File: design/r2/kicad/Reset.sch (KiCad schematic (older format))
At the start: 13 parts, among them IC15 555N, J23 RESET_SW

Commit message: Tidy up footprints
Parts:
- removed J23: RESET_SW, Connector_PinHeader_2.54mm:PinHeader_2x01_P2.54mm_Vertical, symbol Connector:Conn_01x02_Male
- C20: footprint rosco_m68k:C-Electolytic-2,5-5 -> rosco_m68k:E2,5-5
- R27, R28, R29, R30, R31, R32: footprint rosco_m68k:R-0207_10 -> rosco_m68k:0207_10
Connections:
- wire segments 53 -> 47
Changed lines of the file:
@@
 $Descr A4 11693 8268
 encoding utf-8
-Sheet 5 7
+Sheet 4 7
 Title "rosco_m68k Pro (030) Prototype"
 Date "2021-10-01"
@@
 	7450 3200 7450 3000
 Wire Wire Line
-	3350 5200 3450 5200
-Wire Wire Line
 	3850 3800 4150 3800
 Wire Wire Line
@@
 Wire Wire Line
 	1650 4900 1650 3400
-Wire Wire Line
-	2950 5200 2650 5200
 Wire Wire Line
 	2350 5200 2350 4900
@@
 F 0 "R27" V 2191 2750 59  0000 L BNN
 F 1 "2K2" V 2080 2750 59  0000 L BNN
-F 2 "rosco_m68k:R-0207_10" H 2050 2700 50  0001 C CNN
+F 2 "rosco_m68k:0207_10" H 2050 2700 50  0001 C CNN
 F 3 "" H 2050 2700 50  0001 C CNN
 	1    2050 2700
@@
 F 0 "R28" H 3700 5050 59  0000 L BNN
 F 1 "270R" H 3650 5300 59  0000 L BNN
-F 2 "rosco_m68k:R-0207_10" H 3750 5200 50  0001 C CNN
+F 2 "rosco_m68k:0207_10" H 3750 5200 50  0001 C CNN
 F 3 "" H 3750 5200 50  0001 C CNN
 	1    3750 5200
@@
 F 0 "R30" V 8191 2850 59  0000 L BNN
 F 1 "330R" V 8080 2850 59  0000 L BNN
-F 2 "rosco_m68k:R-0207_10" H 8050 2800 50  0001 C CNN
+F 2 "rosco_m68k:0207_10" H 8050 2800 50  0001 C CNN
 F 3 "" H 8050 2800 50  0001 C CNN
 	1    8050 2800
@@
 F 0 "R31" V 8641 2850 59  0000 L BNN
 F 1 "4K7" V 8530 2850 59  0000 L BNN
-F 2 "rosco_m68k:R-0207_10" H 8500 2800 50  0001 C CNN
+F 2 "rosco_m68k:0207_10" H 8500 2800 50  0001 C CNN
 F 3 "" H 8500 2800 50  0001 C CNN
 	1    8500 2800
@@
 F 0 "R32" V 9291 2850 59  0000 L BNN
 F 1 "4K7" V 9180 2850 59  0000 L BNN
-F 2 "rosco_m68k:R-0207_10" H 9150 2800 50  0001 C CNN
+F 2 "rosco_m68k:0207_10" H 9150 2800 50  0001 C CNN
 F 3 "" H 9150 2800 50  0001 C CNN
 	1    9150 2800
@@
 F 0 "R29" V 7591 2850 59  0000 L BNN
 F 1 "330R" V 7480 2850 59  0000 L BNN
-F 2 "rosco_m68k:R-0207_10" H 7450 2800 50  0001 C CNN
+F 2 "rosco_m68k:0207_10" H 7450 2800 50  0001 C CNN
 F 3 "" H 7450 2800 50  0001 C CNN
 	1    7450 2800
@@
 AR Path="/60FBFA5C/6104F05A" Ref="LED?"  Part="1"
 AR Path="/61043B8D/6104F05A" Ref="LED2"  Part="1"
-AR Path="/6162E38E/6104F05A" Ref="LED2"  Part="1"
-F 0 "LED2" H 8300 3400 59  0000 R TNN
+AR Path="/6162E38E/6104F05A" Ref="LED4"  Part="1"
+F 0 "LED4" H 8300 3400 59  0000 R TNN
 F 1 "RED" H 8300 3300 59  0000 R TNN
 F 2 "rosco_m68k:LED5MM" H 8050 3300 50  0001 C CNN
@@
 AR Path="/60FBFA5C/6104F060" Ref="LED?"  Part="1"
 AR Path="/61043B8D/6104F060" Ref="LED1"  Part="1"
-AR Path="/6162E38E/6104F060" Ref="LED1"  Part="1"
-F 0 "LED1" H 7700 3400 59  0000 R TNN
+AR Path="/6162E38E/6104F060" Ref="LED3"  Part="1"
+F 0 "LED3" H 7700 3400 59  0000 R TNN
 F 1 "GREEN" H 7800 3300 59  0000 R TNN
 F 2 "rosco_m68k:LED5MM" H 7450 3300 50  0001 C CNN
@@
 F 0 "C11" H 2095 4119 59  0000 L BNN
 F 1 "100uF" H 2095 3919 59  0000 L BNN
-F 2 "rosco_m68k:C-Electolytic-2,5-5" H 2050 4100 50  0001 C CNN
+F 2 "rosco_m68k:E2,5-5" H 2050 4100 50  0001 C CNN
 F 3 "" H 2050 4100 50  0001 C CNN
 	1    2050 4100
@@
 Wire Wire Line
 	4500 4800 4800 4800
-Connection ~ 2650 5200
-Wire Wire Line
-	2650 5200 2350 5200
-$Comp
-L Connector:Conn_01x02_Male J23
-U 1 1 6172EF3B
-P 3200 5600
-F 0 "J23" V 3500 5500 50  0000 L CNN
-F 1 "RESET_SW" V 3600 5350 50  0000 L CNN
-F 2 "Connector_PinHeader_2.54mm:PinHeader_2x01_P2.54mm_Vertical" H 3200 5600 50  0001 C CNN
-F 3 "~" H 3200 5600 50  0001 C CNN
-	1    3200 5600
-	0    1    1    0
-$EndComp
-Wire Wire Line
-	3100 5800 2650 5800
-Wire Wire Line
-	2650 5200 2650 5800
-Wire Wire Line
-	3200 5800 3450 5800
-Wire Wire Line
-	3450 5800 3450 5200
-Connection ~ 3450 5200
-Wire Wire Line
-	3450 5200 3550 5200
 Text GLabel 4800 4800 2    50   Output ~ 0
 HWRST
@@
 Text GLabel 6100 3700 0    50   Input ~ 0
 RUNLED
+Wire Wire Line
+	2350 5200 2950 5200
+Wire Wire Line
+	3350 5200 3550 5200
 $EndSCHEMATC

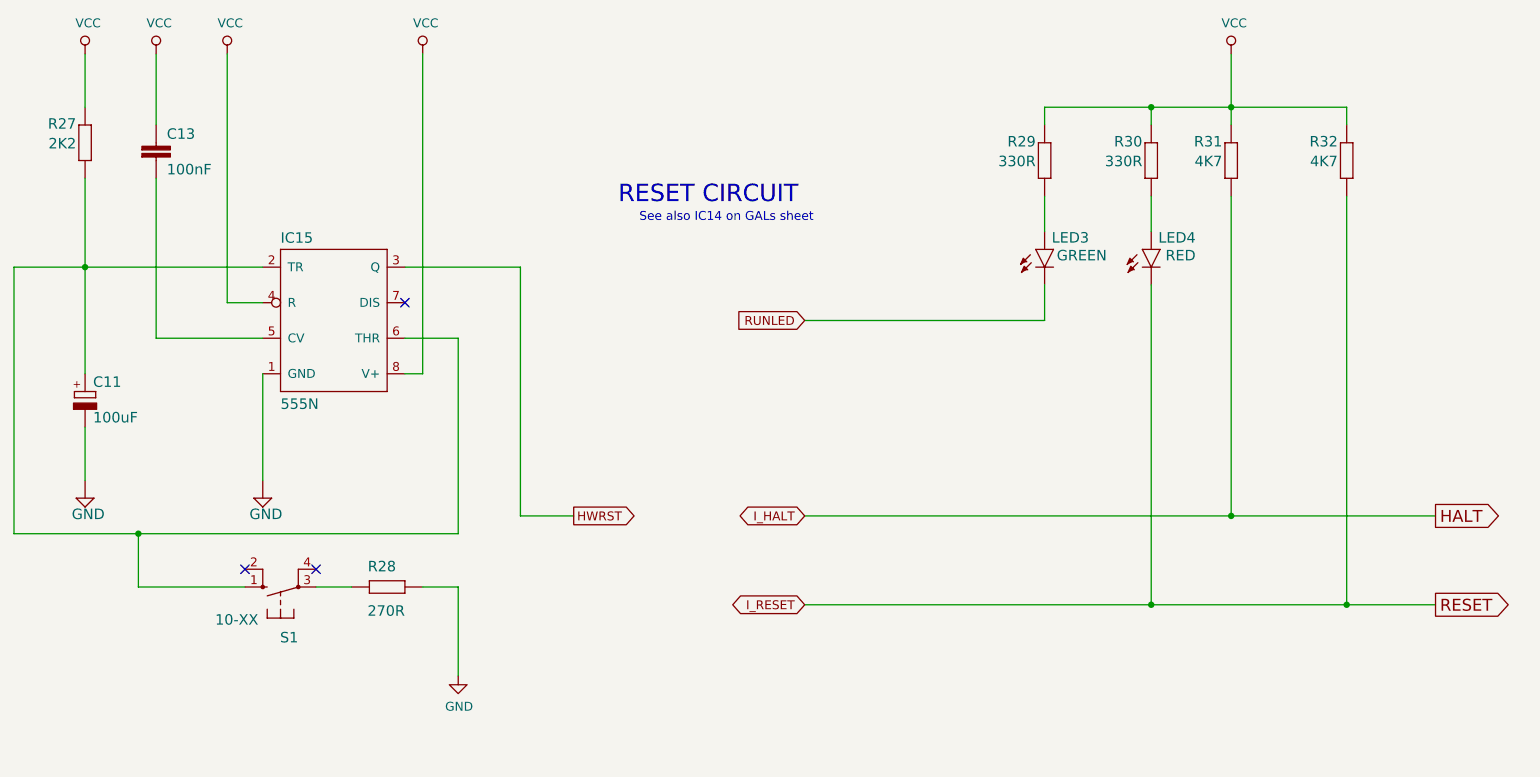
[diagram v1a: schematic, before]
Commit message: Schematic / GAL tweaks and do layout
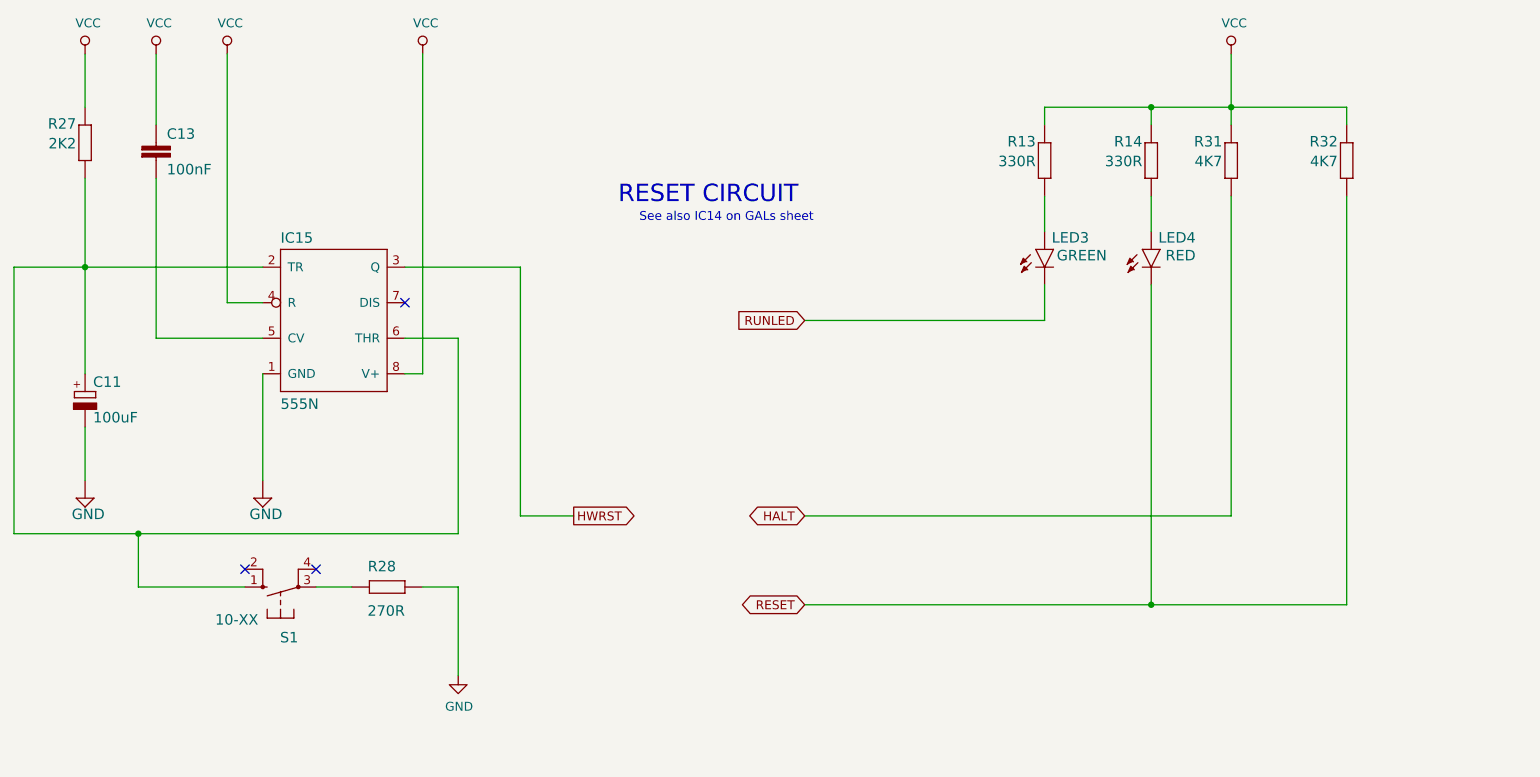
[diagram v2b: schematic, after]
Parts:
- C21: footprint Capacitor_THT:C_Rect_L4.0mm_W2.5mm_P2.50mm -> rosco_m68k:C2.5-3
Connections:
- net I_RESET renamed RESET
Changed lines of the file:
@@
 Wire Wire Line
 	2450 3800 3050 3800
-Text GLabel 9650 4800 2    67   Output ~ 0
-HALT
 Wire Wire Line
 	7450 3700 7450 3500
@@
 Connection ~ 2050 3400
 Connection ~ 2350 4900
-Text GLabel 9650 5300 2    67   Output ~ 0
-RESET
 $Comp
 L rosco_m68k-eagle-import:555N IC?
@@
 AR Path="/60FBFA5C/6104F030" Ref="R?"  Part="1"
 AR Path="/61043B8D/6104F030" Ref="R30"  Part="1"
-AR Path="/6162E38E/6104F030" Ref="R30"  Part="1"
-F 0 "R30" V 8191 2850 59  0000 L BNN
+AR Path="/6162E38E/6104F030" Ref="R14"  Part="1"
+F 0 "R14" V 8191 2850 59  0000 L BNN
 F 1 "330R" V 8080 2850 59  0000 L BNN
 F 2 "rosco_m68k:0207_10" H 8050 2800 50  0001 C CNN
@@
 	1    9150 2800
 	0    -1   -1   0
-$EndComp
-$Comp
-L rosco_m68k-eagle-import:R-EU_0207_10 R?
-U 1 1 6104F042
-P 7450 2800
-AR Path="/6104F042" Ref="R?"  Part="1"
-AR Path="/5E53B952/6104F042" Ref="R?"  Part="1"
-AR Path="/60FBFA5C/6104F042" Ref="R?"  Part="1"
-AR Path="/61043B8D/6104F042" Ref="R29"  Part="1"
-AR Path="/6162E38E/6104F042" Ref="R29"  Part="1"
-F 0 "R29" V 7591 2850 59  0000 L BNN
-F 1 "330R" V 7480 2850 59  0000 L BNN
-F 2 "rosco_m68k:0207_10" H 7450 2800 50  0001 C CNN
-F 3 "" H 7450 2800 50  0001 C CNN
-	1    7450 2800
-	0    -1   -1   0
-$EndComp
-$Comp
-L rosco_m68k-eagle-import:C2,5-3 C?
-U 1 1 6104F048
-P 2450 2700
-AR Path="/6104F048" Ref="C?"  Part="1"
-AR Path="/5E53B952/6104F048" Ref="C?"  Part="1"
-AR Path="/60FBFA5C/6104F048" Ref="C?"  Part="1"
-AR Path="/61043B8D/6104F048" Ref="C21"  Part="1"
-AR Path="/6162E38E/6104F048" Ref="C13"  Part="1"
-F 0 "C13" H 2510 2715 59  0000 L BNN
-F 1 "100nF" H 2510 2515 59  0000 L BNN
-F 2 "Capacitor_THT:C_Rect_L4.0mm_W2.5mm_P2.50mm" H 2450 2700 50  0001 C CNN
-F 3 "" H 2450 2700 50  0001 C CNN
-	1    2450 2700
-	1    0    0    -1
 $EndComp
 $Comp
@@
 Wire Wire Line
 	8500 3000 8500 4800
-Connection ~ 8500 4800
-Wire Wire Line
-	8500 4800 9650 4800
 Wire Wire Line
 	7450 2500 8050 2500
@@
 Wire Wire Line
 	8050 3000 8050 3200
-Connection ~ 9150 5300
-Wire Wire Line
-	9150 5300 9650 5300
 Wire Wire Line
 	8500 2500 9150 2500
@@
 	6100 3700 7450 3700
 Text GLabel 6100 5300 0    50   3State ~ 0
-I_RESET
+RESET
 Text GLabel 6100 4800 0    50   3State ~ 0
-I_HALT
+HALT
 Text GLabel 6100 3700 0    50   Input ~ 0
 RUNLED
@@
 Wire Wire Line
 	3350 5200 3550 5200
+$Comp
+L rosco_m68k-eagle-import:R-EU_0207_10 R?
+U 1 1 6104F042
+P 7450 2800
+AR Path="/6104F042" Ref="R?"  Part="1"
+AR Path="/5E53B952/6104F042" Ref="R?"  Part="1"
+AR Path="/60FBFA5C/6104F042" Ref="R?"  Part="1"
+AR Path="/61043B8D/6104F042" Ref="R29"  Part="1"
+AR Path="/6162E38E/6104F042" Ref="R13"  Part="1"
+F 0 "R13" V 7591 2850 59  0000 L BNN
+F 1 "330R" V 7480 2850 59  0000 L BNN
+F 2 "rosco_m68k:0207_10" H 7450 2800 50  0001 C CNN
+F 3 "" H 7450 2800 50  0001 C CNN
+	1    7450 2800
+	0    -1   -1   0
+$EndComp
+$Comp
+L rosco_m68k-eagle-import:C2,5-3 C?
+U 1 1 6104F048
+P 2450 2700
+AR Path="/6104F048" Ref="C?"  Part="1"
+AR Path="/5E53B952/6104F048" Ref="C?"  Part="1"
+AR Path="/60FBFA5C/6104F048" Ref="C?"  Part="1"
+AR Path="/61043B8D/6104F048" Ref="C21"  Part="1"
+AR Path="/6162E38E/6104F048" Ref="C13"  Part="1"
+F 0 "C13" H 2510 2715 59  0000 L BNN
+F 1 "100nF" H 2510 2515 59  0000 L BNN
+F 2 "rosco_m68k:C2.5-3" H 2450 2700 50  0001 C CNN
+F 3 "" H 2450 2700 50  0001 C CNN
+	1    2450 2700
+	1    0    0    -1
+$EndComp
 $EndSCHEMATC
